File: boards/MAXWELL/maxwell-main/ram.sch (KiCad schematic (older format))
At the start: 48 parts, among them U2 XC7K160T-2FFG676C, U3 DDR3_SODIMM

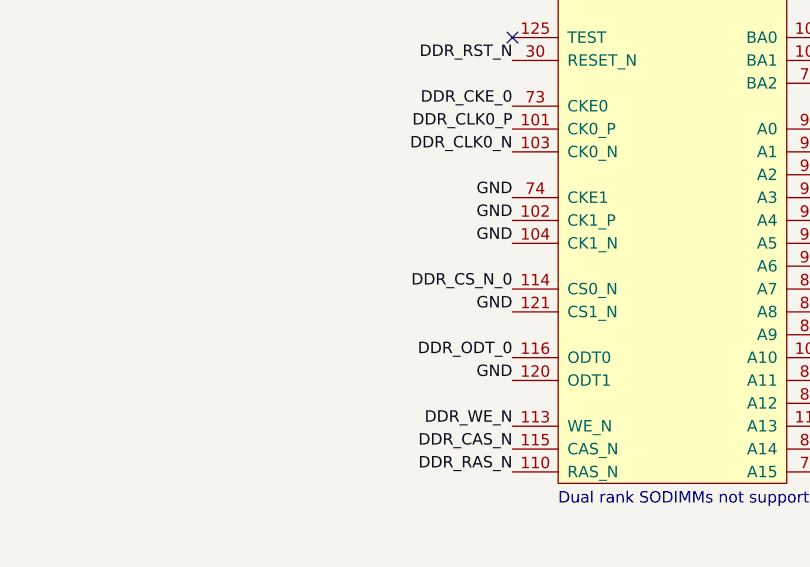
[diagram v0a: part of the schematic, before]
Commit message: Fixed LCD backlight polarity reversed. Added pulldowns instead of direct ground connections to SODIMM unused rank chip select/clock
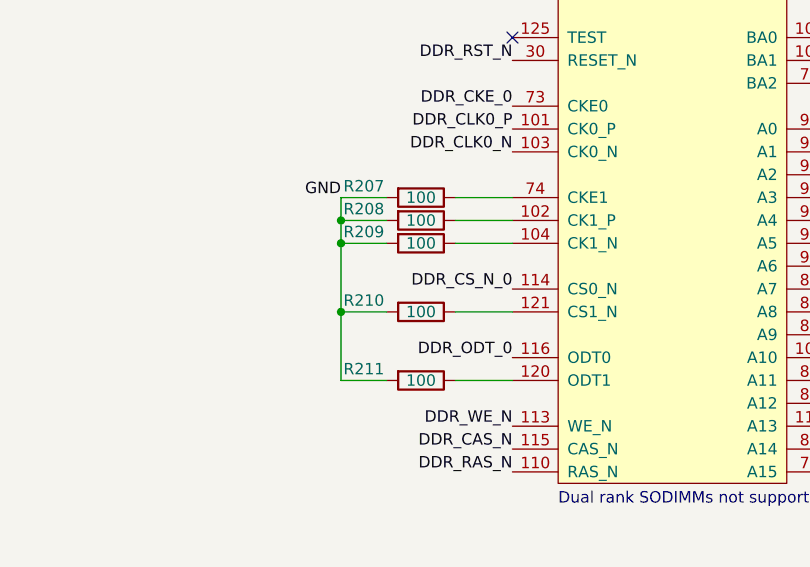
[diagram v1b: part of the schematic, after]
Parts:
- added R207, R208, R209, R210, R211: 100, symbol device:R
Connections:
- net GND: now also R207.2, R208.2, R209.2, R210.2, R211.2; no longer U3.102 (CK1_P), U3.104 (CK1_N), U3.120 (ODT1), U3.121 (CS1_N), U3.74 (CKE1)
- new net: R208.1, U3.102 (CK1_P)
- new net: R209.1, U3.104 (CK1_N)
- new net: R211.1, U3.120 (ODT1)
- new net: R210.1, U3.121 (CS1_N)
- new net: R207.1, U3.74 (CKE1)
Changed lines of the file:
@@
 Text Label 10800 5400 0    50   ~ 0
 GND
-Text Label 13200 7850 2    50   ~ 0
-GND
-Text Label 13200 7550 2    50   ~ 0
-GND
-Text Label 13200 7250 2    50   ~ 0
-GND
-Text Label 13200 7150 2    50   ~ 0
-GND
-Text Label 13200 7050 2    50   ~ 0
+Text Label 12450 7050 2    50   ~ 0
 GND
 Text Notes 13400 8400 0    50   ~ 0
@@
 GND
 NoConn ~ 13200 6350
+$Comp
+L device:R R207
+U 1 1 61D6F8B3
+P 12800 7050
+F 0 "R207" V 12750 6800 50  0000 C CNN
+F 1 "100" V 12800 7050 50  0000 C CNN
+F 2 "" V 12730 7050 50  0001 C CNN
+F 3 "" H 12800 7050 50  0001 C CNN
+	1    12800 7050
+	0    1    1    0
+$EndComp
+$Comp
+L device:R R208
+U 1 1 61D7A2D1
+P 12800 7150
+F 0 "R208" V 12750 6900 50  0000 C CNN
+F 1 "100" V 12800 7150 50  0000 C CNN
+F 2 "" V 12730 7150 50  0001 C CNN
+F 3 "" H 12800 7150 50  0001 C CNN
+	1    12800 7150
+	0    1    1    0
+$EndComp
+$Comp
+L device:R R209
+U 1 1 61D7A4AF
+P 12800 7250
+F 0 "R209" V 12750 7000 50  0000 C CNN
+F 1 "100" V 12800 7250 50  0000 C CNN
+F 2 "" V 12730 7250 50  0001 C CNN
+F 3 "" H 12800 7250 50  0001 C CNN
+	1    12800 7250
+	0    1    1    0
+$EndComp
+Wire Wire Line
+	12650 7050 12450 7050
+Wire Wire Line
+	12450 7150 12650 7150
+Wire Wire Line
+	12650 7250 12450 7250
+Wire Wire Line
+	12950 7050 13200 7050
+Wire Wire Line
+	13200 7150 12950 7150
+Wire Wire Line
+	12950 7250 13200 7250
+$Comp
+L device:R R210
+U 1 1 61D9E87A
+P 12800 7550
+F 0 "R210" V 12750 7300 50  0000 C CNN
+F 1 "100" V 12800 7550 50  0000 C CNN
+F 2 "" V 12730 7550 50  0001 C CNN
+F 3 "" H 12800 7550 50  0001 C CNN
+	1    12800 7550
+	0    1    1    0
+$EndComp
+$Comp
+L device:R R211
+U 1 1 61D9EA9C
+P 12800 7850
+F 0 "R211" V 12750 7600 50  0000 C CNN
+F 1 "100" V 12800 7850 50  0000 C CNN
+F 2 "" V 12730 7850 50  0001 C CNN
+F 3 "" H 12800 7850 50  0001 C CNN
+	1    12800 7850
+	0    1    1    0
+$EndComp
+Wire Wire Line
+	12650 7850 12450 7850
+Wire Wire Line
+	12450 7850 12450 7550
+Connection ~ 12450 7150
+Wire Wire Line
+	12450 7150 12450 7050
+Connection ~ 12450 7250
+Wire Wire Line
+	12450 7250 12450 7150
+Wire Wire Line
+	12650 7550 12450 7550
+Connection ~ 12450 7550
+Wire Wire Line
+	12450 7550 12450 7250
+Wire Wire Line
+	12950 7550 13200 7550
+Wire Wire Line
+	13200 7850 12950 7850
 $EndSCHEMATC

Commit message: Continued schematic review. Added footprints for C1-C282.
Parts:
- C166, C167, C172, C174, C175, C180, C181, C184, C188, C192, C196: footprint (none) -> azonenberg_pcb:EIA_0603_CAP_NOSILK
- C168, C169: footprint (none) -> azonenberg_pcb:EIA_1210_CAP_NOSILK
- C170, C171, C173, C176, C177, C178, C179, C182, C183, C185, C186, C187, C189, C190, C191, C193, C194, C195, C197, C198, C199, C200, C201, C202, C204: footprint (none) -> azonenberg_pcb:EIA_0402_CAP_NOSILK
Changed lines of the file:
@@
 F 0 "C191" H 4765 6996 50  0000 L CNN
 F 1 "0.47 uF" H 4765 6905 50  0000 L CNN
-F 2 "" H 4688 6800 50  0001 C CNN
+F 2 "azonenberg_pcb:EIA_0402_CAP_NOSILK" H 4688 6800 50  0001 C CNN
 F 3 "" H 4650 6950 50  0001 C CNN
 	1    4650 6950
@@
 F 0 "C195" H 5315 6996 50  0000 L CNN
 F 1 "0.47 uF" H 5315 6905 50  0000 L CNN
-F 2 "" H 5238 6800 50  0001 C CNN
+F 2 "azonenberg_pcb:EIA_0402_CAP_NOSILK" H 5238 6800 50  0001 C CNN
 F 3 "" H 5200 6950 50  0001 C CNN
 	1    5200 6950
@@
 F 0 "C178" H 3615 6996 50  0000 L CNN
 F 1 "0.47 uF" H 3615 6905 50  0000 L CNN
-F 2 "" H 3538 6800 50  0001 C CNN
+F 2 "azonenberg_pcb:EIA_0402_CAP_NOSILK" H 3538 6800 50  0001 C CNN
 F 3 "" H 3500 6950 50  0001 C CNN
 	1    3500 6950
@@
 F 0 "C187" H 4165 6996 50  0000 L CNN
 F 1 "0.47 uF" H 4165 6905 50  0000 L CNN
-F 2 "" H 4088 6800 50  0001 C CNN
+F 2 "azonenberg_pcb:EIA_0402_CAP_NOSILK" H 4088 6800 50  0001 C CNN
 F 3 "" H 4050 6950 50  0001 C CNN
 	1    4050 6950
@@
 F 0 "C166" H 2515 6996 50  0000 L CNN
 F 1 "4.7 uF" H 2515 6905 50  0000 L CNN
-F 2 "" H 2438 6800 50  0001 C CNN
+F 2 "azonenberg_pcb:EIA_0603_CAP_NOSILK" H 2438 6800 50  0001 C CNN
 F 3 "" H 2400 6950 50  0001 C CNN
 	1    2400 6950
@@
 F 0 "C172" H 3065 6996 50  0000 L CNN
 F 1 "4.7 uF" H 3065 6905 50  0000 L CNN
-F 2 "" H 2988 6800 50  0001 C CNN
+F 2 "azonenberg_pcb:EIA_0603_CAP_NOSILK" H 2988 6800 50  0001 C CNN
 F 3 "" H 2950 6950 50  0001 C CNN
 	1    2950 6950
@@
 F 0 "C179" H 3615 7646 50  0000 L CNN
 F 1 "0.47 uF" H 3615 7555 50  0000 L CNN
-F 2 "" H 3538 7450 50  0001 C CNN
+F 2 "azonenberg_pcb:EIA_0402_CAP_NOSILK" H 3538 7450 50  0001 C CNN
 F 3 "" H 3500 7600 50  0001 C CNN
 	1    3500 7600
@@
 F 0 "C173" H 3065 7646 50  0000 L CNN
 F 1 "0.47 uF" H 3065 7555 50  0000 L CNN
-F 2 "" H 2988 7450 50  0001 C CNN
+F 2 "azonenberg_pcb:EIA_0402_CAP_NOSILK" H 2988 7450 50  0001 C CNN
 F 3 "" H 2950 7600 50  0001 C CNN
 	1    2950 7600
@@
 F 0 "C167" H 2515 7646 50  0000 L CNN
 F 1 "4.7 uF" H 2515 7555 50  0000 L CNN
-F 2 "" H 2438 7450 50  0001 C CNN
+F 2 "azonenberg_pcb:EIA_0603_CAP_NOSILK" H 2438 7450 50  0001 C CNN
 F 3 "" H 2400 7600 50  0001 C CNN
 	1    2400 7600
@@
 F 0 "C168" H 2515 8246 50  0000 L CNN
 F 1 "100 uF" H 2515 8155 50  0000 L CNN
-F 2 "" H 2438 8050 50  0001 C CNN
+F 2 "azonenberg_pcb:EIA_1210_CAP_NOSILK" H 2438 8050 50  0001 C CNN
 F 3 "" H 2400 8200 50  0001 C CNN
 	1    2400 8200
@@
 F 0 "C174" H 3065 8246 50  0000 L CNN
 F 1 "4.7 uF" H 3065 8155 50  0000 L CNN
-F 2 "" H 2988 8050 50  0001 C CNN
+F 2 "azonenberg_pcb:EIA_0603_CAP_NOSILK" H 2988 8050 50  0001 C CNN
 F 3 "" H 2950 8200 50  0001 C CNN
 	1    2950 8200
@@
 F 0 "C180" H 3615 8246 50  0000 L CNN
 F 1 "4.7 uF" H 3615 8155 50  0000 L CNN
-F 2 "" H 3538 8050 50  0001 C CNN
+F 2 "azonenberg_pcb:EIA_0603_CAP_NOSILK" H 3538 8050 50  0001 C CNN
 F 3 "" H 3500 8200 50  0001 C CNN
 	1    3500 8200
@@
 F 0 "C169" H 2515 8796 50  0000 L CNN
 F 1 "100 uF" H 2515 8705 50  0000 L CNN
-F 2 "" H 2438 8600 50  0001 C CNN
+F 2 "azonenberg_pcb:EIA_1210_CAP_NOSILK" H 2438 8600 50  0001 C CNN
 F 3 "" H 2400 8750 50  0001 C CNN
 	1    2400 8750
@@
 F 0 "C175" H 3065 8796 50  0000 L CNN
 F 1 "4.7 uF" H 3065 8705 50  0000 L CNN
-F 2 "" H 2988 8600 50  0001 C CNN
+F 2 "azonenberg_pcb:EIA_0603_CAP_NOSILK" H 2988 8600 50  0001 C CNN
 F 3 "" H 2950 8750 50  0001 C CNN
 	1    2950 8750
@@
 F 0 "C181" H 3615 8796 50  0000 L CNN
 F 1 "4.7 uF" H 3615 8705 50  0000 L CNN
-F 2 "" H 3538 8600 50  0001 C CNN
+F 2 "azonenberg_pcb:EIA_0603_CAP_NOSILK" H 3538 8600 50  0001 C CNN
 F 3 "" H 3500 8750 50  0001 C CNN
 	1    3500 8750
@@
 F 0 "C184" H 4115 8796 50  0000 L CNN
 F 1 "4.7 uF" H 4115 8705 50  0000 L CNN
-F 2 "" H 4038 8600 50  0001 C CNN
+F 2 "azonenberg_pcb:EIA_0603_CAP_NOSILK" H 4038 8600 50  0001 C CNN
 F 3 "" H 4000 8750 50  0001 C CNN
 	1    4000 8750
@@
 F 0 "C188" H 4615 8796 50  0000 L CNN
 F 1 "4.7 uF" H 4615 8705 50  0000 L CNN
-F 2 "" H 4538 8600 50  0001 C CNN
+F 2 "azonenberg_pcb:EIA_0603_CAP_NOSILK" H 4538 8600 50  0001 C CNN
 F 3 "" H 4500 8750 50  0001 C CNN
 	1    4500 8750
@@
 F 0 "C192" H 5115 8796 50  0000 L CNN
 F 1 "4.7 uF" H 5115 8705 50  0000 L CNN
-F 2 "" H 5038 8600 50  0001 C CNN
+F 2 "azonenberg_pcb:EIA_0603_CAP_NOSILK" H 5038 8600 50  0001 C CNN
 F 3 "" H 5000 8750 50  0001 C CNN
 	1    5000 8750
@@
 F 0 "C196" H 5615 8796 50  0000 L CNN
 F 1 "4.7 uF" H 5615 8705 50  0000 L CNN
-F 2 "" H 5538 8600 50  0001 C CNN
+F 2 "azonenberg_pcb:EIA_0603_CAP_NOSILK" H 5538 8600 50  0001 C CNN
 F 3 "" H 5500 8750 50  0001 C CNN
 	1    5500 8750
@@
 F 0 "C170" H 2515 9346 50  0000 L CNN
 F 1 "0.47 uF" H 2515 9255 50  0000 L CNN
-F 2 "" H 2438 9150 50  0001 C CNN
+F 2 "azonenberg_pcb:EIA_0402_CAP_NOSILK" H 2438 9150 50  0001 C CNN
 F 3 "" H 2400 9300 50  0001 C CNN
 	1    2400 9300
@@
 F 0 "C176" H 3065 9346 50  0000 L CNN
 F 1 "0.47 uF" H 3065 9255 50  0000 L CNN
-F 2 "" H 2988 9150 50  0001 C CNN
+F 2 "azonenberg_pcb:EIA_0402_CAP_NOSILK" H 2988 9150 50  0001 C CNN
 F 3 "" H 2950 9300 50  0001 C CNN
 	1    2950 9300
@@
 F 0 "C182" H 3615 9346 50  0000 L CNN
 F 1 "0.47 uF" H 3615 9255 50  0000 L CNN
-F 2 "" H 3538 9150 50  0001 C CNN
+F 2 "azonenberg_pcb:EIA_0402_CAP_NOSILK" H 3538 9150 50  0001 C CNN
 F 3 "" H 3500 9300 50  0001 C CNN
 	1    3500 9300
@@
 F 0 "C185" H 4115 9346 50  0000 L CNN
 F 1 "0.47 uF" H 4115 9255 50  0000 L CNN
-F 2 "" H 4038 9150 50  0001 C CNN
+F 2 "azonenberg_pcb:EIA_0402_CAP_NOSILK" H 4038 9150 50  0001 C CNN
 F 3 "" H 4000 9300 50  0001 C CNN
 	1    4000 9300
@@
 F 0 "C189" H 4615 9346 50  0000 L CNN
 F 1 "0.47 uF" H 4615 9255 50  0000 L CNN
-F 2 "" H 4538 9150 50  0001 C CNN
+F 2 "azonenberg_pcb:EIA_0402_CAP_NOSILK" H 4538 9150 50  0001 C CNN
 F 3 "" H 4500 9300 50  0001 C CNN
 	1    4500 9300
@@
 F 0 "C193" H 5115 9346 50  0000 L CNN
 F 1 "0.47 uF" H 5115 9255 50  0000 L CNN
-F 2 "" H 5038 9150 50  0001 C CNN
+F 2 "azonenberg_pcb:EIA_0402_CAP_NOSILK" H 5038 9150 50  0001 C CNN
 F 3 "" H 5000 9300 50  0001 C CNN
 	1    5000 9300
@@
 F 0 "C197" H 5615 9346 50  0000 L CNN
 F 1 "0.47 uF" H 5615 9255 50  0000 L CNN
-F 2 "" H 5538 9150 50  0001 C CNN
+F 2 "azonenberg_pcb:EIA_0402_CAP_NOSILK" H 5538 9150 50  0001 C CNN
 F 3 "" H 5500 9300 50  0001 C CNN
 	1    5500 9300
@@
 F 0 "C199" H 6165 9346 50  0000 L CNN
 F 1 "0.47 uF" H 6165 9255 50  0000 L CNN
-F 2 "" H 6088 9150 50  0001 C CNN
+F 2 "azonenberg_pcb:EIA_0402_CAP_NOSILK" H 6088 9150 50  0001 C CNN
 F 3 "" H 6050 9300 50  0001 C CNN
 	1    6050 9300
@@
 F 0 "C201" H 6715 9346 50  0000 L CNN
 F 1 "0.47 uF" H 6715 9255 50  0000 L CNN
-F 2 "" H 6638 9150 50  0001 C CNN
+F 2 "azonenberg_pcb:EIA_0402_CAP_NOSILK" H 6638 9150 50  0001 C CNN
 F 3 "" H 6600 9300 50  0001 C CNN
 	1    6600 9300
@@
 F 0 "C171" H 2515 9896 50  0000 L CNN
 F 1 "0.47 uF" H 2515 9805 50  0000 L CNN
-F 2 "" H 2438 9700 50  0001 C CNN
+F 2 "azonenberg_pcb:EIA_0402_CAP_NOSILK" H 2438 9700 50  0001 C CNN
 F 3 "" H 2400 9850 50  0001 C CNN
 	1    2400 9850
@@
 F 0 "C177" H 3065 9896 50  0000 L CNN
 F 1 "0.47 uF" H 3065 9805 50  0000 L CNN
-F 2 "" H 2988 9700 50  0001 C CNN
+F 2 "azonenberg_pcb:EIA_0402_CAP_NOSILK" H 2988 9700 50  0001 C CNN
 F 3 "" H 2950 9850 50  0001 C CNN
 	1    2950 9850
@@
 F 0 "C183" H 3615 9896 50  0000 L CNN
 F 1 "0.47 uF" H 3615 9805 50  0000 L CNN
-F 2 "" H 3538 9700 50  0001 C CNN
+F 2 "azonenberg_pcb:EIA_0402_CAP_NOSILK" H 3538 9700 50  0001 C CNN
 F 3 "" H 3500 9850 50  0001 C CNN
 	1    3500 9850
@@
 F 0 "C186" H 4115 9896 50  0000 L CNN
 F 1 "0.47 uF" H 4115 9805 50  0000 L CNN
-F 2 "" H 4038 9700 50  0001 C CNN
+F 2 "azonenberg_pcb:EIA_0402_CAP_NOSILK" H 4038 9700 50  0001 C CNN
 F 3 "" H 4000 9850 50  0001 C CNN
 	1    4000 9850
@@
 F 0 "C190" H 4615 9896 50  0000 L CNN
 F 1 "0.47 uF" H 4615 9805 50  0000 L CNN
-F 2 "" H 4538 9700 50  0001 C CNN
+F 2 "azonenberg_pcb:EIA_0402_CAP_NOSILK" H 4538 9700 50  0001 C CNN
 F 3 "" H 4500 9850 50  0001 C CNN
 	1    4500 9850
@@
 F 0 "C194" H 5115 9896 50  0000 L CNN
 F 1 "0.47 uF" H 5115 9805 50  0000 L CNN
-F 2 "" H 5038 9700 50  0001 C CNN
+F 2 "azonenberg_pcb:EIA_0402_CAP_NOSILK" H 5038 9700 50  0001 C CNN
 F 3 "" H 5000 9850 50  0001 C CNN
 	1    5000 9850
@@
 F 0 "C198" H 5615 9896 50  0000 L CNN
 F 1 "0.47 uF" H 5615 9805 50  0000 L CNN
-F 2 "" H 5538 9700 50  0001 C CNN
+F 2 "azonenberg_pcb:EIA_0402_CAP_NOSILK" H 5538 9700 50  0001 C CNN
 F 3 "" H 5500 9850 50  0001 C CNN
 	1    5500 9850
@@
 F 0 "C200" H 6165 9896 50  0000 L CNN
 F 1 "0.47 uF" H 6165 9805 50  0000 L CNN
-F 2 "" H 6088 9700 50  0001 C CNN
+F 2 "azonenberg_pcb:EIA_0402_CAP_NOSILK" H 6088 9700 50  0001 C CNN
 F 3 "" H 6050 9850 50  0001 C CNN
 	1    6050 9850
@@
 F 0 "C202" H 6715 9896 50  0000 L CNN
 F 1 "0.47 uF" H 6715 9805 50  0000 L CNN
-F 2 "" H 6638 9700 50  0001 C CNN
+F 2 "azonenberg_pcb:EIA_0402_CAP_NOSILK" H 6638 9700 50  0001 C CNN
 F 3 "" H 6600 9850 50  0001 C CNN
 	1    6600 9850
@@
 F 0 "C204" H 6615 6996 50  0000 L CNN
 F 1 "0.47 uF" H 6615 6905 50  0000 L CNN
-F 2 "" H 6538 6800 50  0001 C CNN
+F 2 "azonenberg_pcb:EIA_0402_CAP_NOSILK" H 6538 6800 50  0001 C CNN
 F 3 "" H 6500 6950 50  0001 C CNN
 	1    6500 6950

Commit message: Assigned footprints for all resistors
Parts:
- R207, R208, R209, R210, R211, R62, R63, R64, R65, R66, R67, R68, R69: footprint (none) -> azonenberg_pcb:EIA_0402_RES_NOSILK
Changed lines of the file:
@@
 Sheet 6 18
 Title "MAXWELL Main Board"
-Date "2020-06-22"
+Date "2020-06-23"
 Rev "0.1"
 Comp "Antikernel Labs"
@@
 F 0 "R67" V 7500 5550 50  0000 C CNN
 F 1 "80" V 7550 5800 50  0000 C CNN
-F 2 "" V 7480 5800 50  0001 C CNN
+F 2 "azonenberg_pcb:EIA_0402_RES_NOSILK" V 7480 5800 50  0001 C CNN
 F 3 "" H 7550 5800 50  0001 C CNN
 	1    7550 5800
@@
 F 0 "R66" V 7500 650 50  0000 C CNN
 F 1 "80" V 7550 900 50  0000 C CNN
-F 2 "" V 7480 900 50  0001 C CNN
+F 2 "azonenberg_pcb:EIA_0402_RES_NOSILK" V 7480 900 50  0001 C CNN
 F 3 "" H 7550 900 50  0001 C CNN
 	1    7550 900
@@
 F 0 "R64" V 4950 650 50  0000 C CNN
 F 1 "80" V 5000 900 50  0000 C CNN
-F 2 "" V 4930 900 50  0001 C CNN
+F 2 "azonenberg_pcb:EIA_0402_RES_NOSILK" V 4930 900 50  0001 C CNN
 F 3 "" H 5000 900 50  0001 C CNN
 	1    5000 900
@@
 F 0 "R65" V 4950 5550 50  0000 C CNN
 F 1 "80" V 5000 5800 50  0000 C CNN
-F 2 "" V 4930 5800 50  0001 C CNN
+F 2 "azonenberg_pcb:EIA_0402_RES_NOSILK" V 4930 5800 50  0001 C CNN
 F 3 "" H 5000 5800 50  0001 C CNN
 	1    5000 5800
@@
 F 0 "R63" V 1950 5550 50  0000 C CNN
 F 1 "80" V 2000 5800 50  0000 C CNN
-F 2 "" V 1930 5800 50  0001 C CNN
+F 2 "azonenberg_pcb:EIA_0402_RES_NOSILK" V 1930 5800 50  0001 C CNN
 F 3 "" H 2000 5800 50  0001 C CNN
 	1    2000 5800
@@
 F 0 "R62" V 1950 650 50  0000 C CNN
 F 1 "80" V 2000 900 50  0000 C CNN
-F 2 "" V 1930 900 50  0001 C CNN
+F 2 "azonenberg_pcb:EIA_0402_RES_NOSILK" V 1930 900 50  0001 C CNN
 F 3 "" H 2000 900 50  0001 C CNN
 	1    2000 900
@@
 F 0 "R68" V 10600 5000 50  0000 C CNN
 F 1 "100" V 10650 5250 50  0000 C CNN
-F 2 "" V 10580 5250 50  0001 C CNN
+F 2 "azonenberg_pcb:EIA_0402_RES_NOSILK" V 10580 5250 50  0001 C CNN
 F 3 "" H 10650 5250 50  0001 C CNN
 	1    10650 5250
@@
 F 0 "R69" V 10600 5150 50  0000 C CNN
 F 1 "4.7K" V 10650 5400 50  0000 C CNN
-F 2 "" V 10580 5400 50  0001 C CNN
+F 2 "azonenberg_pcb:EIA_0402_RES_NOSILK" V 10580 5400 50  0001 C CNN
 F 3 "" H 10650 5400 50  0001 C CNN
 	1    10650 5400
@@
 F 0 "R207" V 12750 6800 50  0000 C CNN
 F 1 "100" V 12800 7050 50  0000 C CNN
-F 2 "" V 12730 7050 50  0001 C CNN
+F 2 "azonenberg_pcb:EIA_0402_RES_NOSILK" V 12730 7050 50  0001 C CNN
 F 3 "" H 12800 7050 50  0001 C CNN
 	1    12800 7050
@@
 F 0 "R208" V 12750 6900 50  0000 C CNN
 F 1 "100" V 12800 7150 50  0000 C CNN
-F 2 "" V 12730 7150 50  0001 C CNN
+F 2 "azonenberg_pcb:EIA_0402_RES_NOSILK" V 12730 7150 50  0001 C CNN
 F 3 "" H 12800 7150 50  0001 C CNN
 	1    12800 7150
@@
 F 0 "R209" V 12750 7000 50  0000 C CNN
 F 1 "100" V 12800 7250 50  0000 C CNN
-F 2 "" V 12730 7250 50  0001 C CNN
+F 2 "azonenberg_pcb:EIA_0402_RES_NOSILK" V 12730 7250 50  0001 C CNN
 F 3 "" H 12800 7250 50  0001 C CNN
 	1    12800 7250
@@
 F 0 "R210" V 12750 7300 50  0000 C CNN
 F 1 "100" V 12800 7550 50  0000 C CNN
-F 2 "" V 12730 7550 50  0001 C CNN
+F 2 "azonenberg_pcb:EIA_0402_RES_NOSILK" V 12730 7550 50  0001 C CNN
 F 3 "" H 12800 7550 50  0001 C CNN
 	1    12800 7550
@@
 F 0 "R211" V 12750 7600 50  0000 C CNN
 F 1 "100" V 12800 7850 50  0000 C CNN
-F 2 "" V 12730 7850 50  0001 C CNN
+F 2 "azonenberg_pcb:EIA_0402_RES_NOSILK" V 12730 7850 50  0001 C CNN
 F 3 "" H 12800 7850 50  0001 C CNN
 	1    12800 7850

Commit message: Began assigning IC footprints
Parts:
- U2: footprint (none) -> azonenberg_pcb:BGA_676_27x27_FULLARRAY_1MM_FFG676
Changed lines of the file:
@@
 F 0 "U2" H 7900 5800 50  0000 L CNN
 F 1 "XC7K160T-2FFG676C" H 7900 5700 50  0000 L CNN
-F 2 "" H 7900 5850 50  0001 C CNN
+F 2 "azonenberg_pcb:BGA_676_27x27_FULLARRAY_1MM_FFG676" H 7900 5850 50  0001 C CNN
 F 3 "" H 7900 5850 50  0001 C CNN
 	11   7900 5850
@@
 F 0 "U2" H 5350 5800 50  0000 L CNN
 F 1 "XC7K160T-2FFG676C" H 5350 5700 50  0000 L CNN
-F 2 "" H 5350 5850 50  0001 C CNN
+F 2 "azonenberg_pcb:BGA_676_27x27_FULLARRAY_1MM_FFG676" H 5350 5850 50  0001 C CNN
 F 3 "" H 5350 5850 50  0001 C CNN
 	10   5350 5850
@@
 F 0 "U2" H 2350 5800 50  0000 L CNN
 F 1 "XC7K160T-2FFG676C" H 2350 5700 50  0000 L CNN
-F 2 "" H 2350 5850 50  0001 C CNN
+F 2 "azonenberg_pcb:BGA_676_27x27_FULLARRAY_1MM_FFG676" H 2350 5850 50  0001 C CNN
 F 3 "" H 2350 5850 50  0001 C CNN
 	9    2350 5850

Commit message: Added footprints for most ICs other than DC-DC modules
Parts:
- U3: footprint (none) -> azonenberg_pcb:CONN_SODIMM_DDR3_TE_2013289-1
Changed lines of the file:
@@
 F 0 "U3" H 13900 10975 50  0000 C CNN
 F 1 "DDR3_SODIMM" H 13900 10884 50  0000 C CNN
-F 2 "" H 13650 8250 50  0001 C CNN
+F 2 "azonenberg_pcb:CONN_SODIMM_DDR3_TE_2013289-1" H 13650 8250 50  0001 C CNN
 F 3 "" H 13650 8250 50  0001 C CNN
 	2    13400 8300
@@
 F 0 "U3" H 13900 10425 50  0000 C CNN
 F 1 "DDR3_SODIMM" H 13900 10334 50  0000 C CNN
-F 2 "" H 13650 5500 50  0001 C CNN
+F 2 "azonenberg_pcb:CONN_SODIMM_DDR3_TE_2013289-1" H 13650 5500 50  0001 C CNN
 F 3 "" H 13650 5500 50  0001 C CNN
 	3    13400 5550
@@
 F 0 "U3" H 10800 9025 50  0000 C CNN
 F 1 "DDR3_SODIMM" H 10800 8934 50  0000 C CNN
-F 2 "" H 10550 4800 50  0001 C CNN
+F 2 "azonenberg_pcb:CONN_SODIMM_DDR3_TE_2013289-1" H 10550 4800 50  0001 C CNN
 F 3 "" H 10550 4800 50  0001 C CNN
 	1    10300 4850

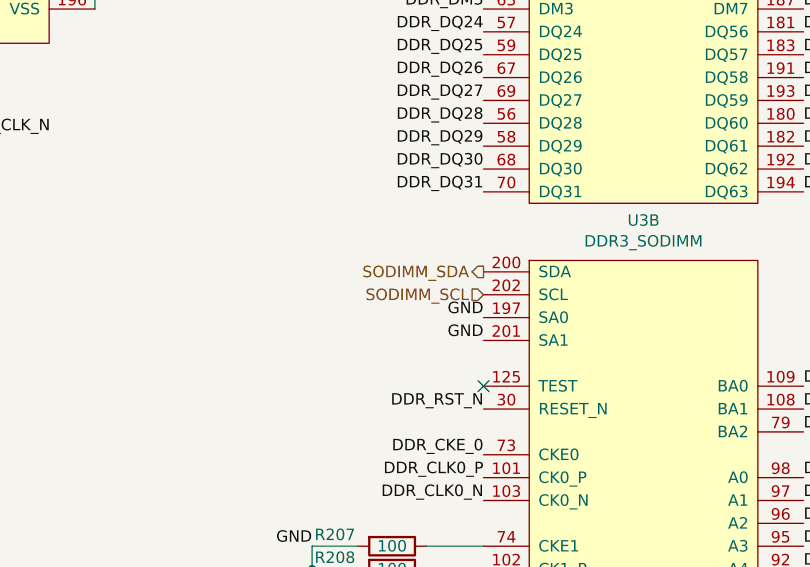
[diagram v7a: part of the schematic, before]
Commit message: Renamed I2C buses to be consistent
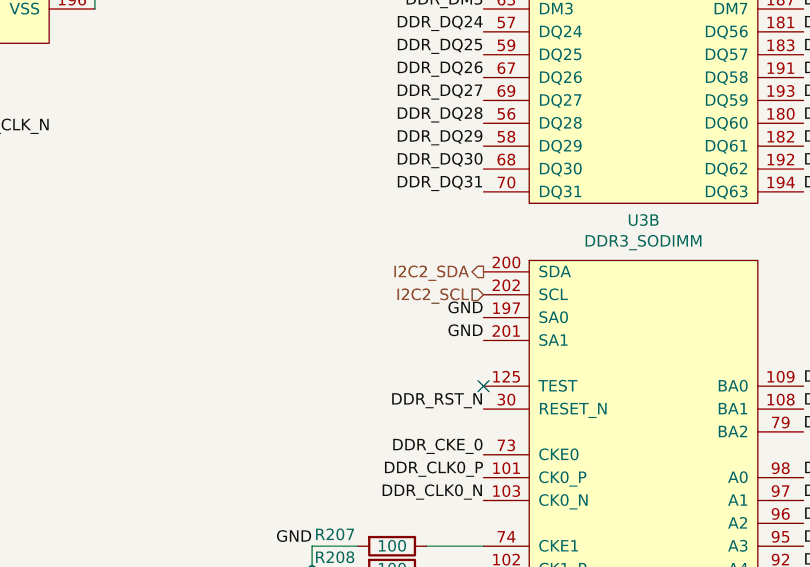
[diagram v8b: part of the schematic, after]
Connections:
- net SODIMM_SCL renamed I2C2_SCL
- net SODIMM_SDA renamed I2C2_SDA
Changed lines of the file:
@@
 NoConn ~ 5150 3400
 Text HLabel 13200 5850 0    50   Output ~ 0
-SODIMM_SDA
+I2C2_SDA
 Text HLabel 13200 5950 0    50   Input ~ 0
-SODIMM_SCL
+I2C2_SCL
 Text Label 13200 6050 2    50   ~ 0
 GND
